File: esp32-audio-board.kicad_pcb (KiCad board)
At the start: 4 copper layers, 45 x 70 mm, 124 parts, among them IC1 XC6220A331MR-G, IC2 XC6220A331MR-G, J1 EN_PAD0, J10 PWR_LED+, J11 HP_LOUT1, J12 HP_ROUT1, J13 HP_LOUT2, J14 HP_ROUT2, J15 MIC_LIN1, J16 MIC_LIN1_GND, J17 MIC_RIN1, J18 MIC_RIN1_GND, J19 HP_1GND, J2 Conn_01x02_Pin, J20 HP_2GND, J21 VP_PAD0, J22 PWR_LED-, J23 CHG_LED+, J24 CHG_LED-, J3 USB_C_Receptacle_USB2.0_16P, J4 EN_PAD1, J5 VP_PAD1, J6 VN_PAD0, J7 VN_PAD1, J8 IO34_PAD0, J9 IO34_PAD1, Q1 SS8050, Q2 SS8050, Q4 AO3401A, U1 ESP32-WROOM-32E, U2 CP2102, U3 MCP73831-2-OT, U5 ES8388

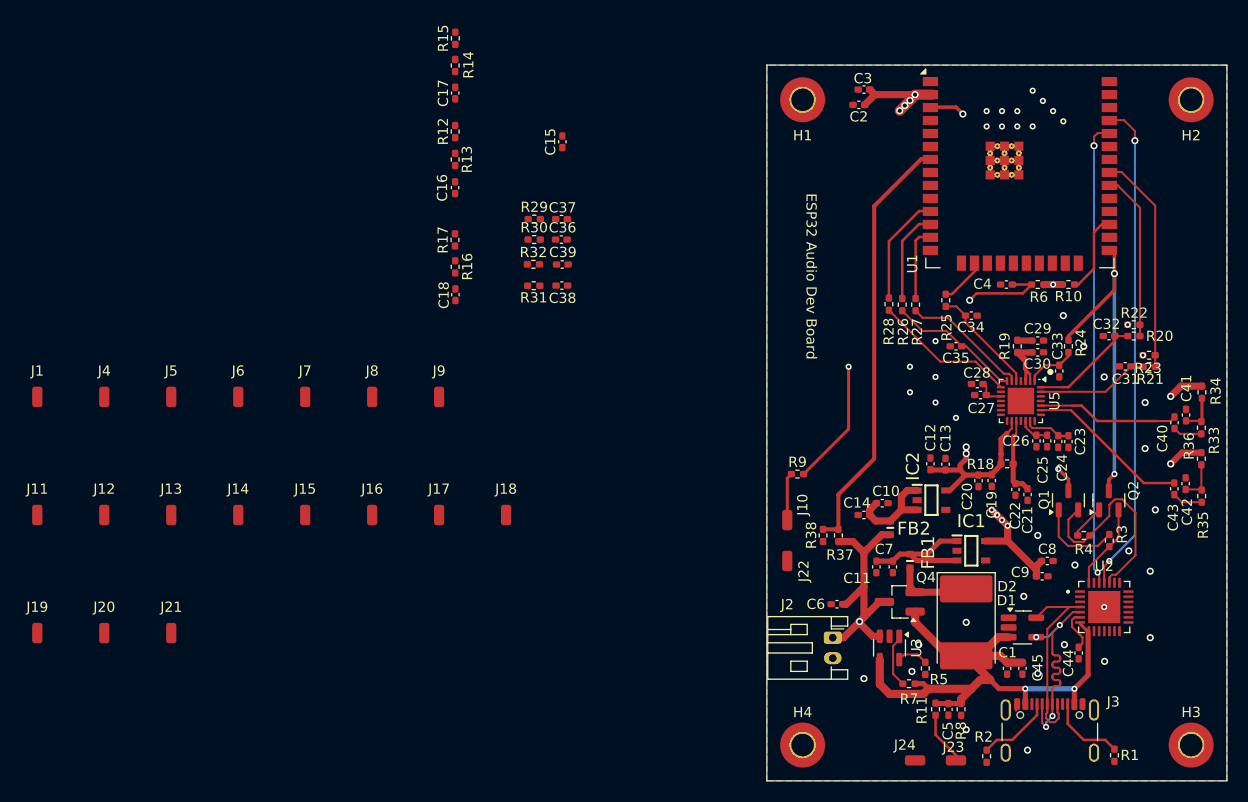
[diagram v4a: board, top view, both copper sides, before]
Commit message: esp32-audio-board: complete PCB
Added all the pads and connections for external input
and output. Made the board smaller to allow the case
to be slimmer.

Signed-off-by: RaresCon <rares.constantin2002@gmail.com>
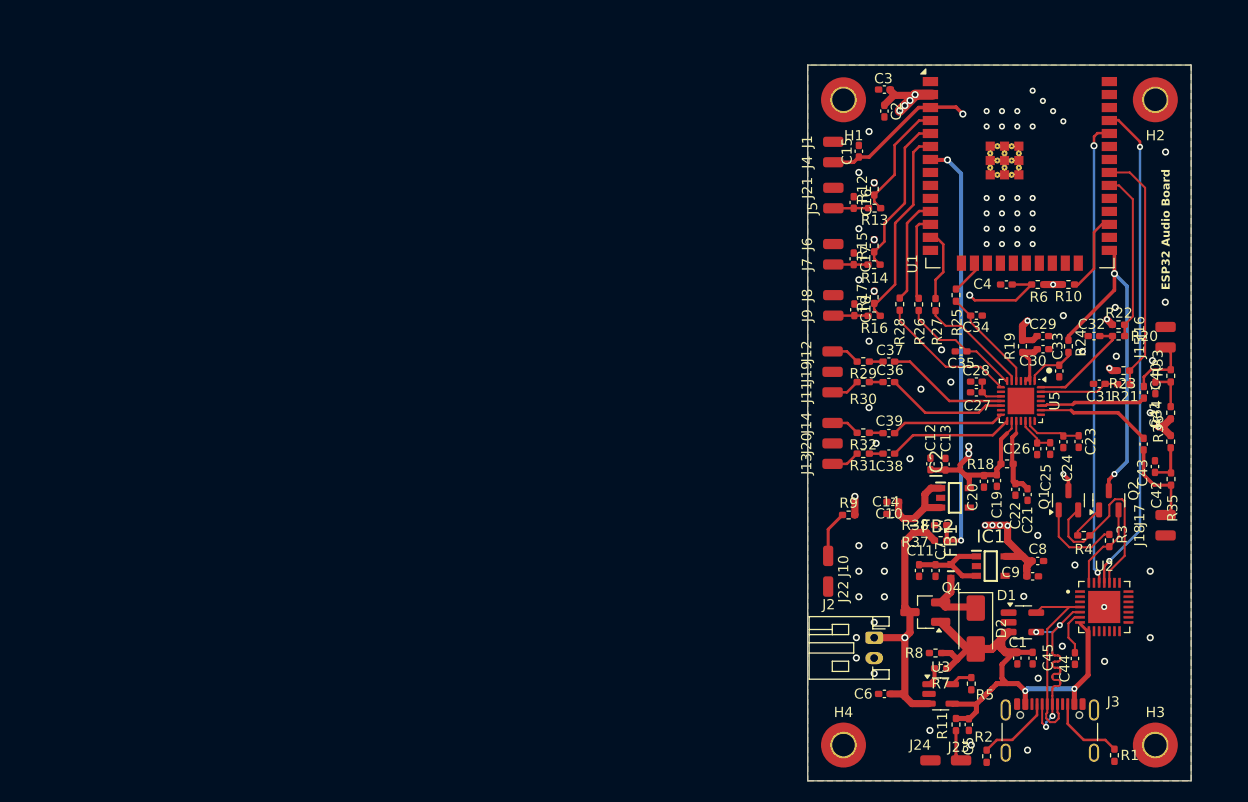
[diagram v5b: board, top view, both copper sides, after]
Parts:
- D2: value D_Schottky -> 3A/10V/280mV; footprint Diode_SMD:D_3220_8050Metric_Pad2.65x5.15mm_HandSolder -> Diode_SMD:D_SMA
- moved J15 85.7 mm to (230.5, 111.1), turned to 90 degrees
- moved J19 81.9 mm to (197.9, 113.5), turned to 90 degrees
- moved J1 81.8 mm to (198.0, 91.0), turned to 90 degrees
- moved J16 79.7 mm to (230.5, 109.1), turned to 90 degrees
- moved J11 78.7 mm to (197.9, 115.5), turned to 90 degrees
- moved J21 78.0 mm to (198.0, 95.5), turned to 90 degrees
- moved J4 74.9 mm to (198.0, 93.0), turned to 90 degrees
- moved J20 73.6 mm to (197.9, 120.5), turned to 90 degrees
- moved J12 73.0 mm to (197.9, 111.5), turned to 90 degrees
- moved J17 71.1 mm to (230.5, 127.5), turned to 90 degrees
- moved J5 67.3 mm to (198.0, 97.5), turned to 90 degrees
- moved J13 64.9 mm to (197.9, 122.5), turned to 90 degrees
- moved J18 64.5 mm to (230.5, 129.5), turned to 90 degrees
- moved J6 60.1 mm to (198.0, 101.0), turned to 90 degrees
- moved J14 58.8 mm to (197.9, 118.5), turned to 90 degrees
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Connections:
- net BAT_LVL renamed ESP_IO35
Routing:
- net ESP_IO34: track 0.00 -> 19.8 mm
- net ESP_SENSOR_VN: track 0.00 -> 16.0 mm
- net VBUS: track 61.1 -> 48.3 mm
- net ES8388_LOUT2: track 0.00 -> 12.3 mm
- net ES8388_ROUT1: track 0.00 -> 12.0 mm
- net ES8388_LOUT1: track 0.00 -> 11.9 mm
- net ESP-EN: track 53.0 -> 64.9 mm
- net ESP_SENSOR_VP: track 0.00 -> 11.9 mm
- net ES8388_ROUT2: track 0.00 -> 11.1 mm
- net Net-(J17-Pin_1): track 3.07 -> 8.67 mm
- net ES8388_RIN1: track 16.0 -> 11.2 mm
- net Net-(IC1-CE): track 13.6 -> 8.95 mm
- net Net-(U3-STAT): track 5.28 -> 1.77 mm
- net Net-(J15-Pin_1): track 2.84 -> 6.34 mm
- net ES8388_LIN1: track 13.9 -> 10.4 mm
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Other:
- board size 45 x 70 mm -> 37.5 x 70 mm
- board text added: "ESP32 Audio Board"
- board text removed: "ESP32 Audio Dev Board"

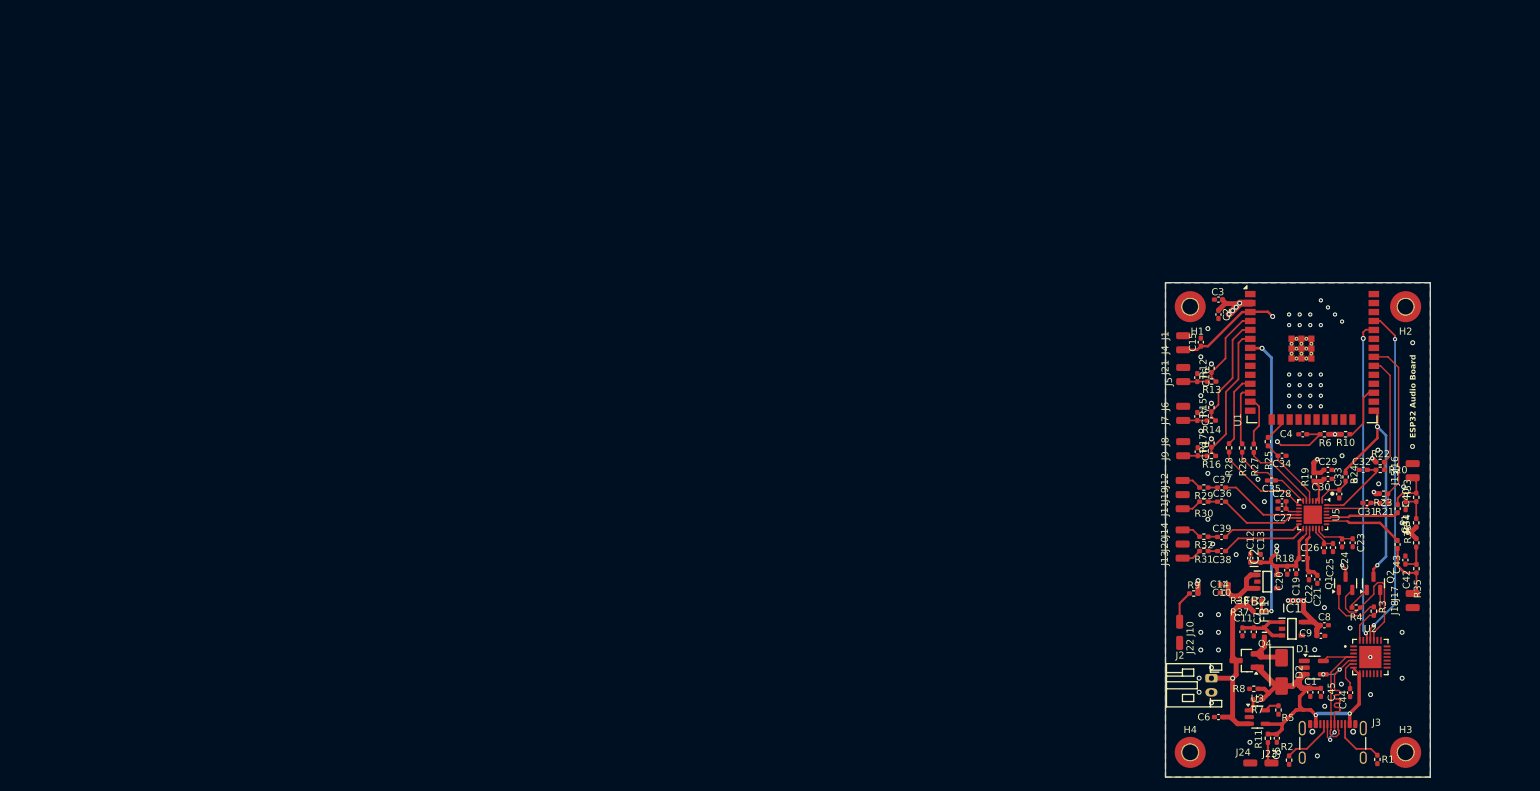
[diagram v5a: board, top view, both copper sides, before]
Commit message: esp32-audio-board: PCB improvements
Rerouted the buttons pins to not use the SENSOR_VN
and SENSOR_VP pins, avoiding any problems with not
being able to pull-up/down them. Added all the
silkscreen texts and reduced the DRC warnings to 1
(silkscreen overlap).

Signed-off-by: RaresCon <rares.constantin2002@gmail.com>
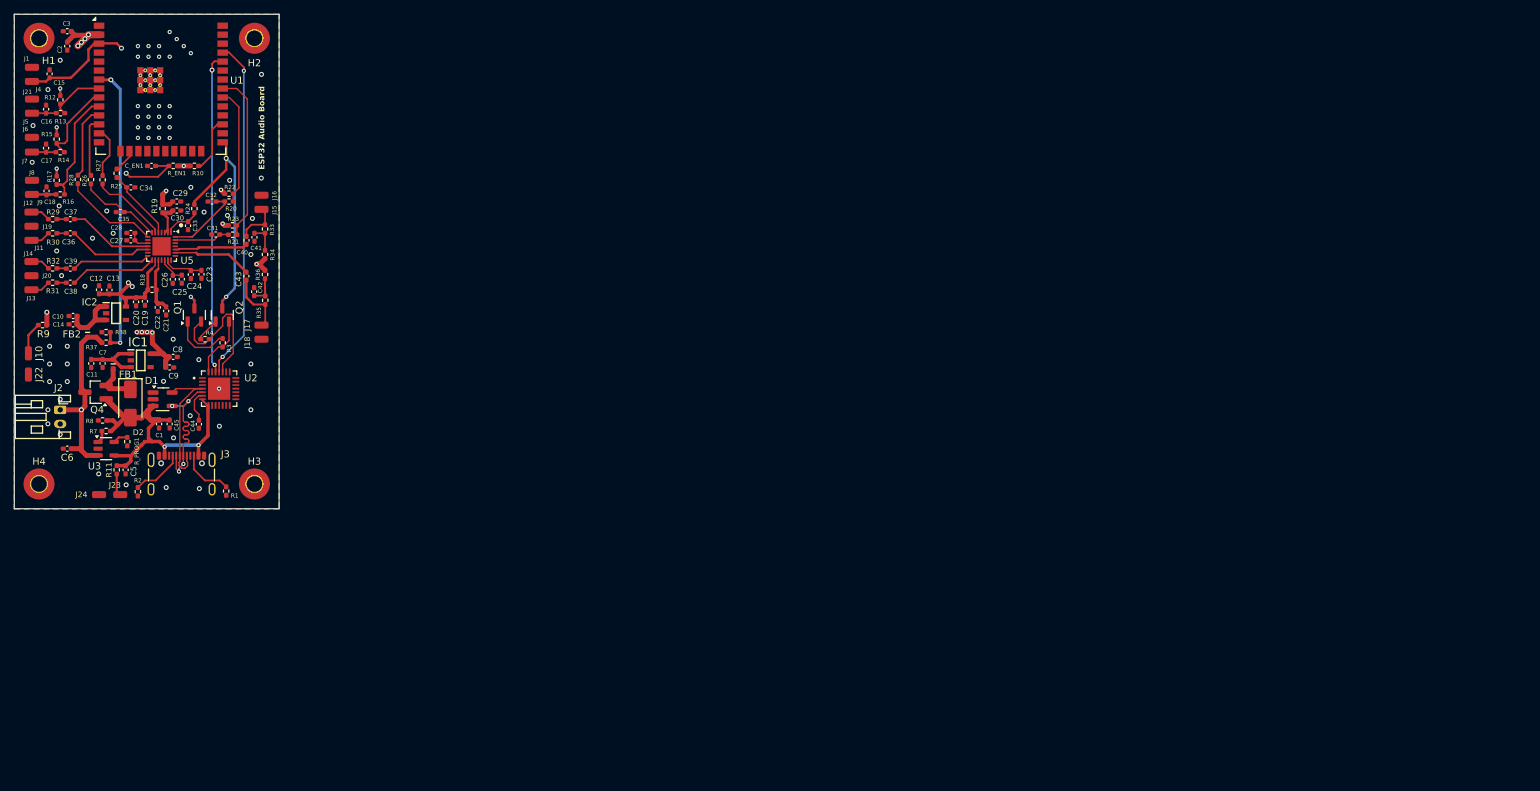
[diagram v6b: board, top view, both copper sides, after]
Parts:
- C1, C10, C12, C15, C16, C17, C18, C19, C22, C3, C30, C44, C7, C9: value 0.1uF -> 0.1uF/1%
- C11, C13, C14, C20, C21, C29, C41, C42, C45, C8: value 10uF -> 10uF/1%
- C2, C36, C37, C38, C39: value 22uF -> 22uF/1%
- C31, C32, C33, C34, C35: value 20pF -> 20pF/1%
- C40, C43: value 1uF -> 1uF/1%
- C5, C6: value 4.7uF -> 4.7uF/1%
- C_EN1: renamed from C4; value 0.1uF -> 0.1uF/1%
- D2: value 3A/10V/280mV -> 3A/20V Schottky Rectifier - MBRA320
- J2: value Conn_01x02_Pin -> JST S2B
- R1: value 5.1K -> 5.1K/1%
- R10: value 10K -> 10K/1%
- R11, R34, R36, R9: value 1K -> 1K/1%
- R13, R14, R16, R19, R20, R21: value 100R -> 100R/1%
- R18: value 4.7R -> 4.7R/1%
- R2: value 5.1K -> 5.1K/%1
- R24, R25, R26, R27, R28, R29, R30, R31, R32: value 33R -> 33R/1%
- R33, R35: value 2K -> 2K/1%
- R7: value 1K -> 1K/%1
- R_EN1: renamed from R6; value 10K -> 10K/1%
- R_PROG1: renamed from R5; value 2K -> 2K/1%
- moved R15 167.9 mm to (38.5, 63.2)
- moved R17 167.7 mm to (38.5, 69.0)
- moved J6 167.4 mm to (35.0, 62.9)
- moved C1 167.4 mm to (53.0, 103.5)
- moved C10 167.4 mm to (40.8, 88.2)
- moved C11 167.4 mm to (43.4, 94.9)
- moved C12 167.4 mm to (44.5, 84.5)
- moved C13 167.4 mm to (46.0, 84.5)
- moved C14 167.4 mm to (40.8, 89.4)
- moved C15 167.4 mm to (37.5, 53.9)
- moved C16 167.4 mm to (37.0, 58.9)
- moved C17 167.4 mm to (37.0, 64.4)
- moved C19 167.4 mm to (51.0, 86.1)
- moved C2 167.4 mm to (40.0, 50.0)
- moved C20 167.4 mm to (49.7, 86.2)
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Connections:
- R12 pad 1: ESP_SENSOR_VP -> ESP_IO32
- R13 pad 1: ESP_SENSOR_VP -> ESP_IO32
- R14 pad 1: ESP_SENSOR_VN -> ESP_IO33
- R15 pad 1: ESP_SENSOR_VN -> ESP_IO33
- R16 pad 1: ESP_IO34 -> ESP_IO25
- R17 pad 1: ESP_IO34 -> ESP_IO25
- U1 pad 10: unconnected-(U1-IO25-Pad10) -> ESP_IO25
- U1 pad 4: ESP_SENSOR_VP -> unconnected-(U1-SENSOR_VP-Pad4)
- U1 pad 5: ESP_SENSOR_VN -> unconnected-(U1-SENSOR_VN-Pad5)
- U1 pad 6: ESP_IO34 -> unconnected-(U1-IO34-Pad6)
- U1 pad 8: unconnected-(U1-IO32-Pad8) -> ESP_IO32
- U1 pad 9: unconnected-(U1-IO33-Pad9) -> ESP_IO33
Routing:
- net ESP_IO34: track 19.8 -> 0.00 mm
- net ESP_IO25: track 0.00 -> 17.0 mm
- net ESP_SENSOR_VN: track 16.0 -> 0.00 mm
- net ESP_SENSOR_VP: track 11.9 -> 0.00 mm
- net ESP_IO33: track 0.00 -> 11.8 mm
- net ESP_IO32: track 0.00 -> 8.09 mm
- net +3V3: track 116.4 -> 119.8 mm
- net ESP-EN: track 64.9 -> 65.8 mm
- net +3V3 Audio: track 76.5 -> 75.8 mm
- net GND: vias 68 -> 69

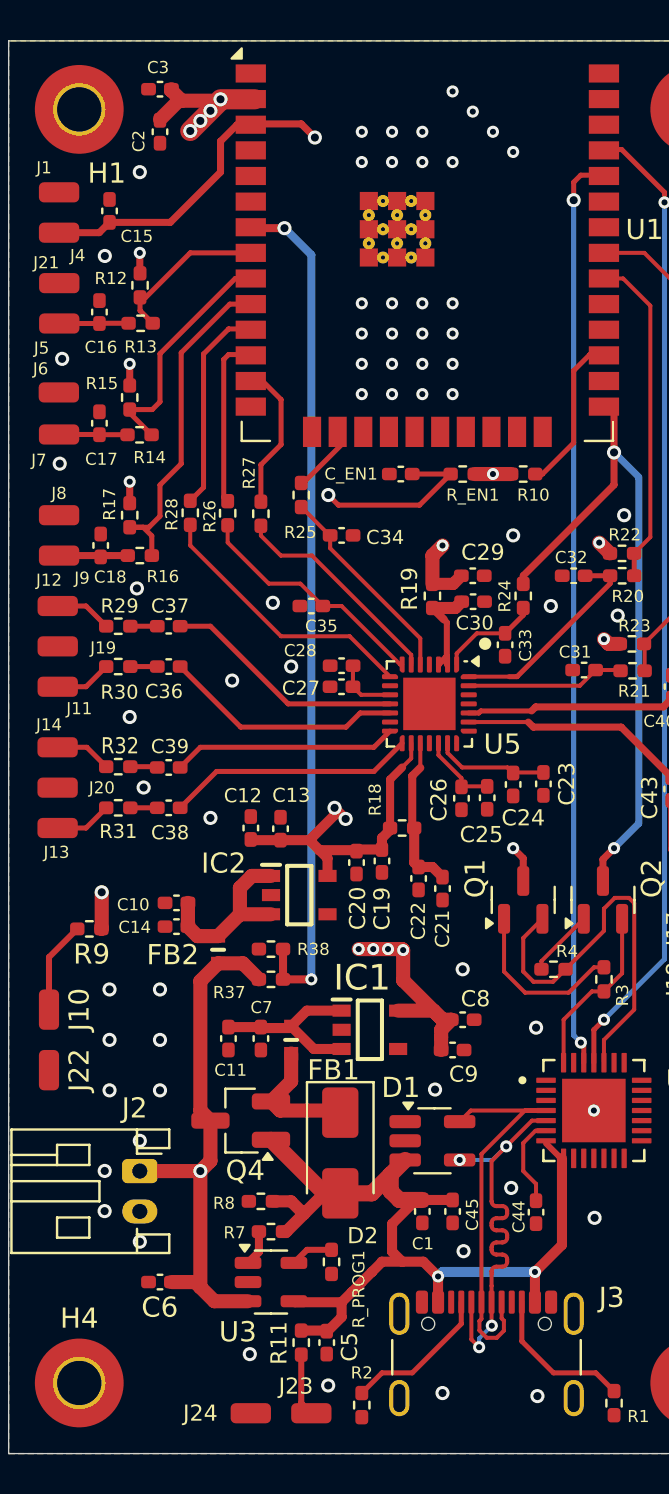
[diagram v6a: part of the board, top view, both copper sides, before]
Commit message: esp32-audio-board: power changes
Changed the LDOs to make the PCB more power
efficient and try to find these parts in stock.
Changed the footprint for the Q4 to be more compact.

Signed-off-by: RaresCon <rares.constantin2002@gmail.com>
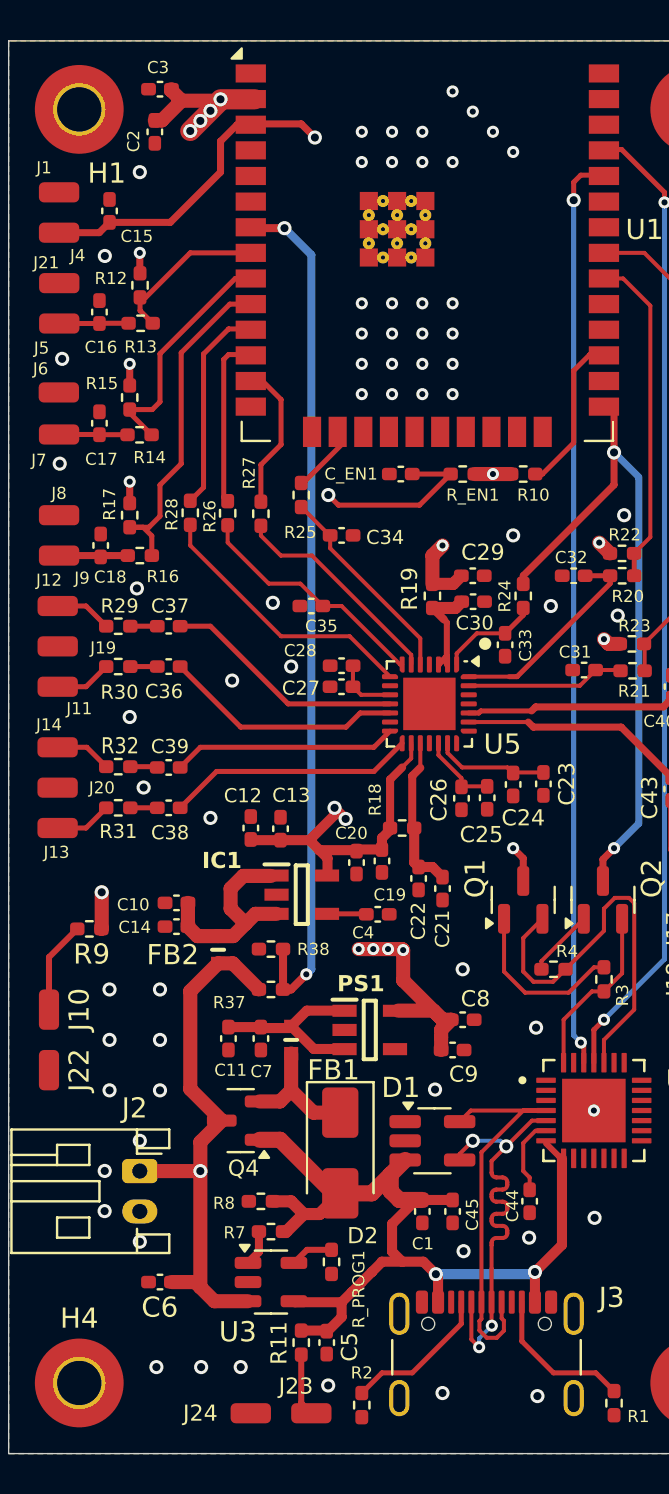
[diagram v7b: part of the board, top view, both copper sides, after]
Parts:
- removed IC2: XC6220A331MR-G, xc6220a331:SOT95P280X120-5N
- added C4: 0.01uF/10%, Capacitor_SMD:C_0402_1005Metric_Pad0.74x0.62mm_HandSolder, F.Cu at (50.8, 88.8)
- added PS1: TLV75733PDBVR, tlv75733pdbvr:SOT95P280X145-5N, F.Cu at (50.4, 94.5)
- C1, C10, C12, C15, C16, C17, C18, C19, C22, C3, C30, C44, C7, C9: value 0.1uF/1% -> 0.1uF/10%
- C11, C13, C14, C20, C21, C29, C41, C42, C45, C8: value 10uF/1% -> 10uF/10%
- C2, C36, C37, C38, C39: value 22uF/1% -> 22uF/10%
- C23, C25, C27: value 10uF -> 10uF/10%
- C24, C26, C28: value 0.1uF -> 0.1uF/10%
- C31, C32, C33, C34, C35: value 20pF/1% -> 20pF/5%
- C40, C43: value 1uF/1% -> 1uF/10%
- C5, C6: value 4.7uF/1% -> 4.7uF/10%
- C_EN1: value 0.1uF/1% -> 1uF/10%
- IC1: value XC6220A331MR-G -> LP2985A-33DBVR; footprint xc6220a331:SOT95P280X120-5N -> lp2985a-33dbvr:SOT95P280X145-5N
- J19: value HP_1GND -> HP_GND1
- J20: value HP_2GND -> HP_GND2
- Q4: footprint Package_TO_SOT_SMD:SOT-23_Handsoldering -> Package_TO_SOT_SMD:SOT-23
- R3, R4: value 10K -> 10K/1%
- R37, R38: value 100K -> 100K/1%
- moved IC1 7.50 mm to (47.0, 87.8)
- moved C44 0.63 mm to (58.3, 103.0)
- moved R37 0.50 mm to (45.5, 92.5)
- moved C2 0.26 mm to (39.7, 50.0)
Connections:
- C10 pad 1: Net-(IC2-CE) -> Net-(IC1-ON/~{OFF})
- C11 pad 1: Net-(IC1-CE) -> Net-(PS1-EN)
- C14 pad 1: Net-(IC2-CE) -> Net-(IC1-ON/~{OFF})
- C7 pad 1: Net-(IC1-CE) -> Net-(PS1-EN)
- FB1 pad 2: Net-(IC1-CE) -> Net-(PS1-EN)
- FB2 pad 2: Net-(IC2-CE) -> Net-(IC1-ON/~{OFF})
- IC1 pad 1: Net-(IC1-CE) -> Net-(IC1-ON/~{OFF})
- IC1 pad 3: Net-(IC1-CE) -> Net-(IC1-ON/~{OFF})
- IC1 pad 4: unconnected-(IC1-NC-Pad4) -> Net-(IC1-BYPASS)
- IC1 pad 5: +3V3 -> +3V3 Audio
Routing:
- net Net-(IC1-ON/~{OFF}): track 0.00 -> 10.5 mm
- net Net-(IC2-CE): track 9.03 -> 0.00 mm
- net Net-(PS1-EN): track 0.00 -> 8.95 mm
- net Net-(IC1-CE): track 8.95 -> 0.00 mm
- net Net-(IC1-BYPASS): track 0.00 -> 1.96 mm
- net VBUS: track 48.3 -> 49.7 mm
- net VBAT: track 26.4 -> 27.5 mm
- net Net-(U2-VDD): track 4.50 -> 3.83 mm
- net GND: vias 69 -> 71
